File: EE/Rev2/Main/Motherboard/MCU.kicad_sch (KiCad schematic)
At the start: 21 parts, among them J7 TAG_CONNECT, U1 STM32G431K6Tx, Y1 Crystal

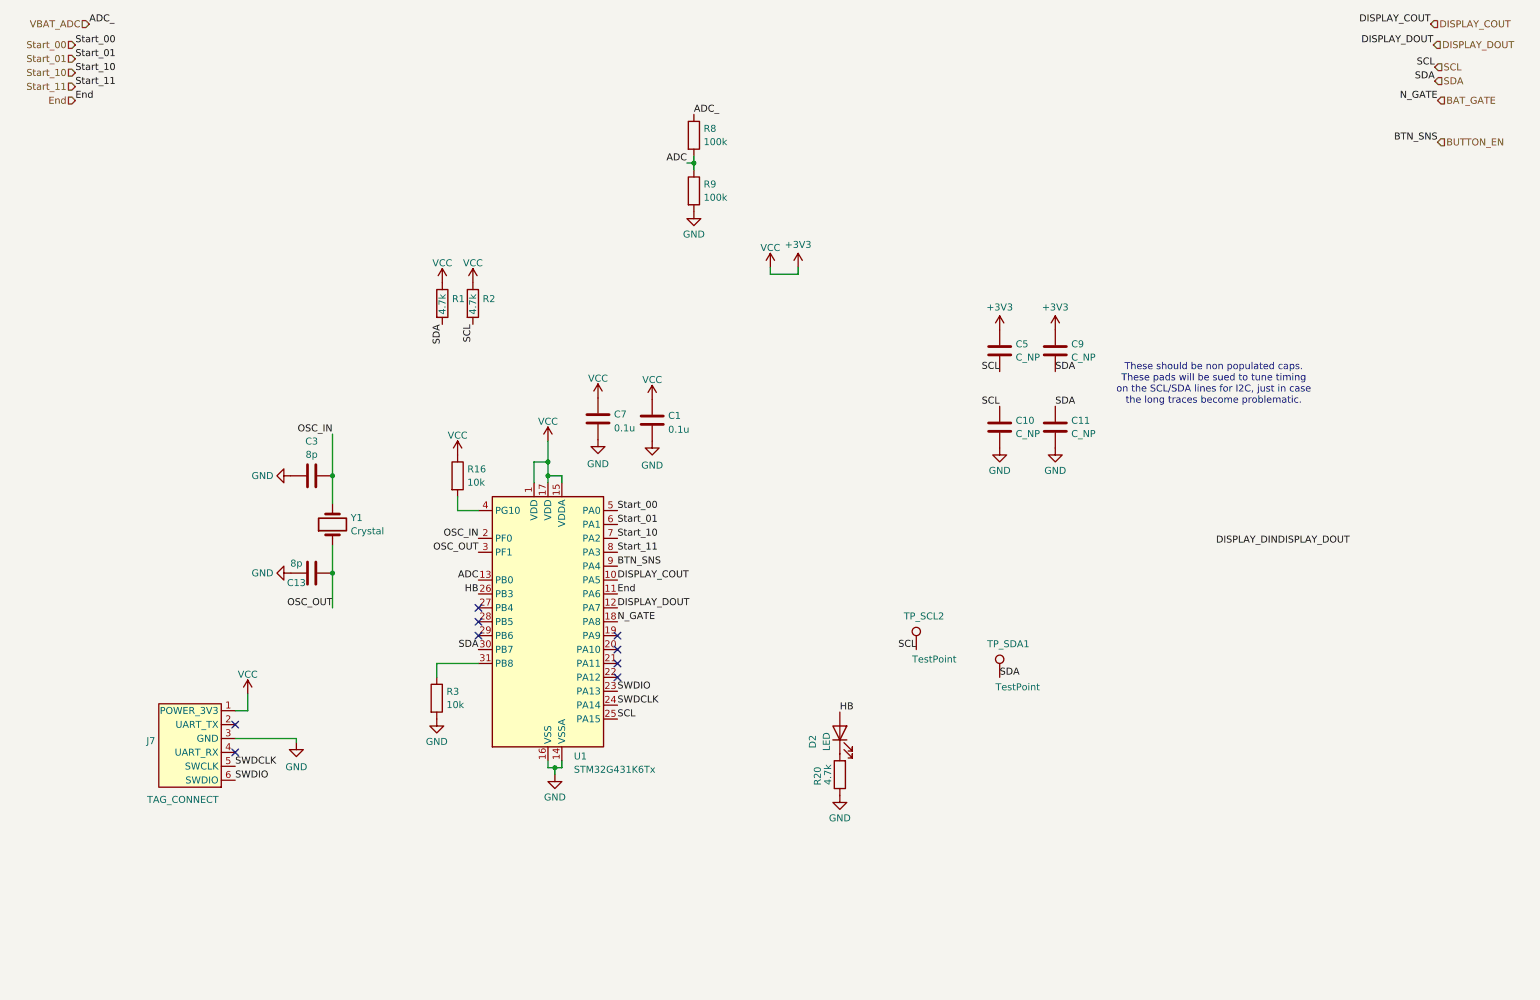
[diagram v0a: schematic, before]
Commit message: Updating Format, Adding Rev2 Start
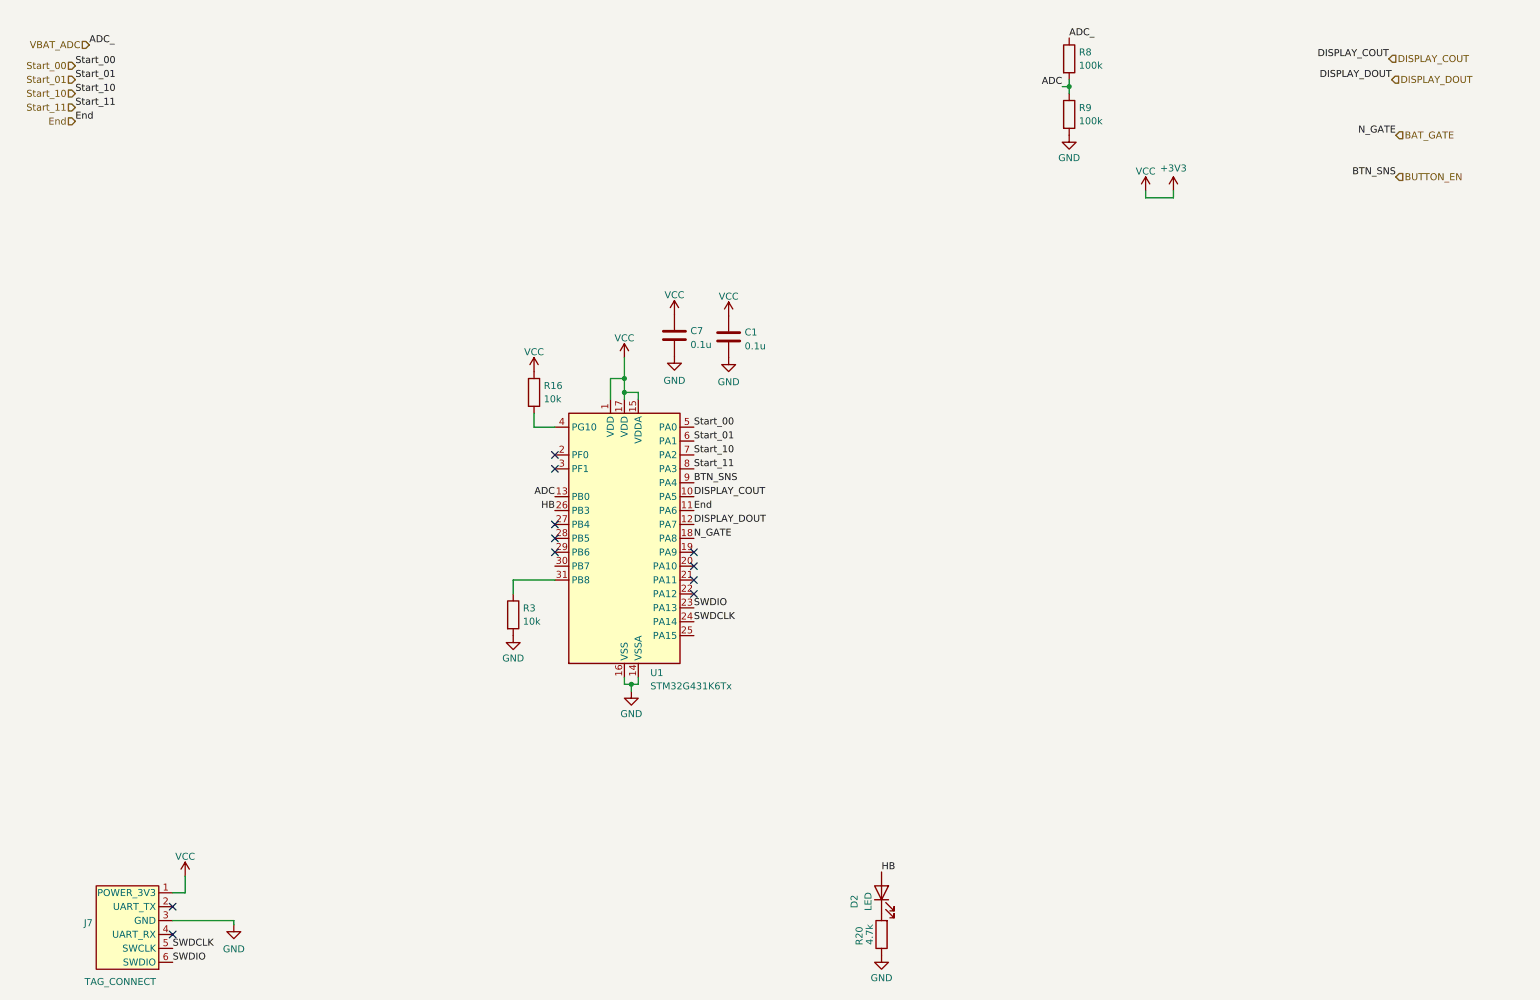
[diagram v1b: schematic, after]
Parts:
- removed C10, C11, C5, C9: C_NP, Capacitor_SMD:C_0402_1005Metric_Pad0.74x0.62mm_HandSolder, symbol Device:C
- removed C13, C3: 8p, Capacitor_SMD:C_0402_1005Metric, symbol Device:C
- removed R1, R2: 4.7k, Resistor_SMD:R_0402_1005Metric, symbol Device:R
- removed TP_SCL2, TP_SDA1: TestPoint, TestPoint:TestPoint_Pad_1.5x1.5mm, symbol Connector:TestPoint
- removed Y1: Crystal, Crystal:Crystal_SMD_5032-2Pin_5.0x3.2mm_HandSoldering, symbol Device:Crystal
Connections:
- net OSC_IN: no longer names the net of U1.2 (PF0)
- net OSC_OUT: no longer names the net of U1.3 (PF1)
- net SCL: no longer names the net of U1.25 (PA15)
- net SDA: no longer names the net of U1.30 (PB7)
- no-connect marks 9 -> 11
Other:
- note removed: "These should be non populated caps. These pads will be sued to tune timing on the SCL/SDA lines for I2C, just in case the long traces become problematic."
- moved on the sheet: C1, C7, D2, J7, R16, R20, R3, R8, R9, U1
